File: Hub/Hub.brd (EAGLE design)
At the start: 85.9 x 24.9 mm, 9 parts

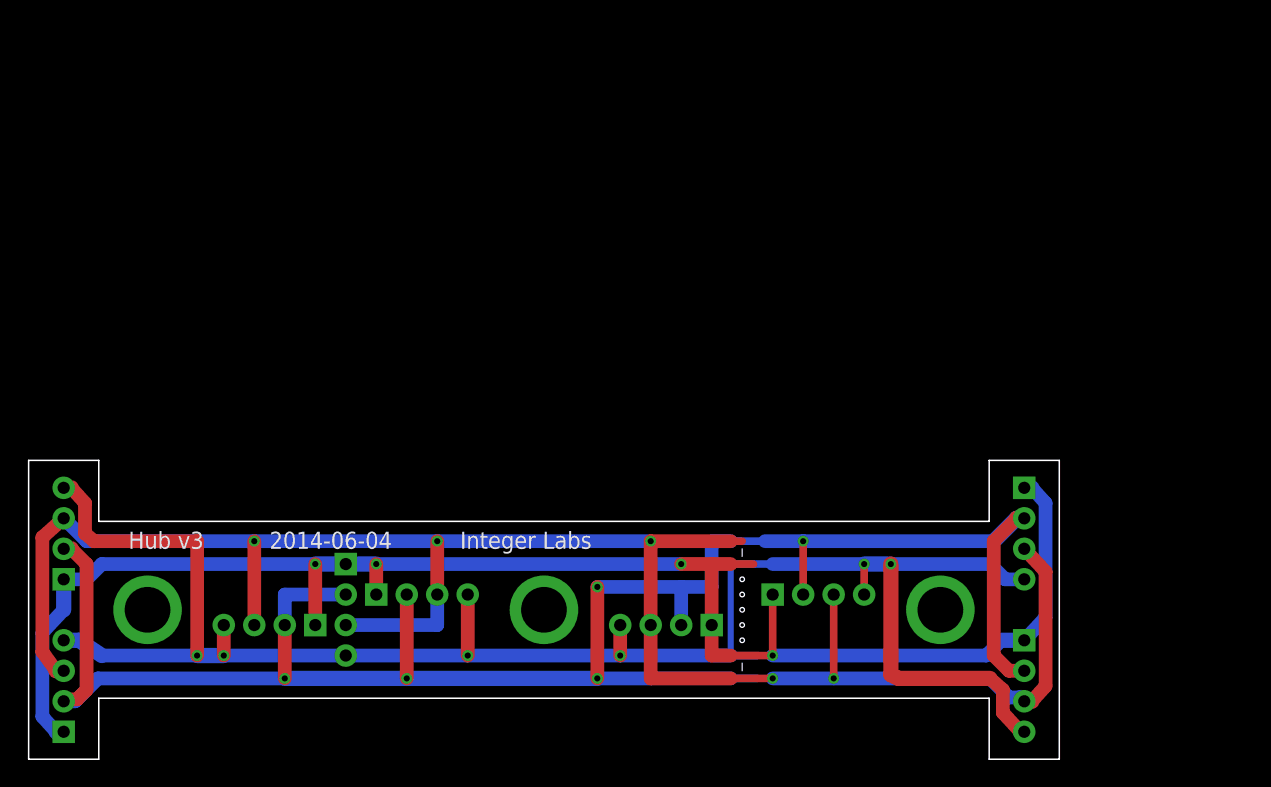
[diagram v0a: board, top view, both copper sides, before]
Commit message: Cleaned up pcb repository file structure.
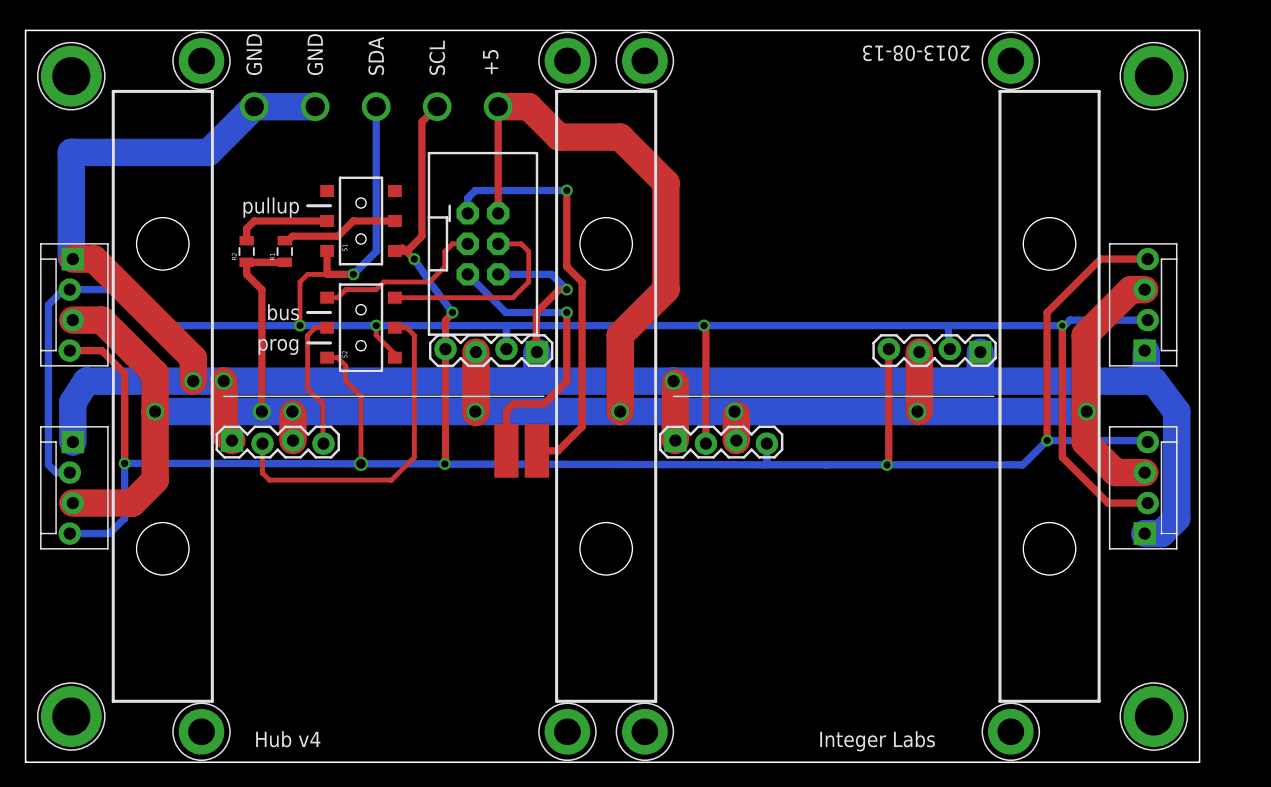
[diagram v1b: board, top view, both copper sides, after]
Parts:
- removed JP5, JP7, JP8: (no value), SparkFun-Connectors:1X04_NO_SILK
- added JP11, JP14: (no value), SparkFun-Connectors:1X04_LOCK
- added JP13: (no value), SparkFun-Connectors:2X3-SHROUDED
- added R1, R2: (no value), SparkFun-Resistors:0805
- added S1, S2: DPDT, SparkFun-Electromechanical:AYZ0202
- added U$1, U$2: SPRING-CONNECTOR, IntegerLabs:SPRING-CONNECTOR
- added U$10, U$11, U$12, U$13, U$14, U$7, U$8, U$9: HOLE#2, IntegerLabs:HOLE-#2
- added U$15, U$16, U$17, U$18, U$19: HOLETEST, IntegerLabs:HOLE-TEST
- added U$3, U$4, U$5, U$6: HOLE#4, IntegerLabs:HOLE-#4
- JP1, JP4: device SparkFun-Connectors:1X04_NO_SILK -> SparkFun-Connectors:1X04_LOCK
- JP2, JP3, JP6, JP9: device SparkFun-Connectors:1X04_NO_SILK -> SparkFun-Connectors:MOLEX-1X4_LOCK
- moved JP2 67.3 mm to (93.3, 34.3), turned to 90 degrees
- moved JP3 37.0 mm to (93.3, 19.1), turned to 90 degrees
- moved JP4 28.3 mm to (42.6, 34.3), turned to 180 degrees
- moved JP6 26.7 mm to (3.81, 41.9), turned to 270 degrees
- moved JP9 25.0 mm to (3.81, 26.7)
- moved JP1 16.7 mm to (17.2, 26.7), turned to 0 degrees
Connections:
- removed net N$1: JP1.4, JP2.4, JP3.4, JP4.4, JP5.4, JP6.4, JP7.4, JP8.4, JP9.4
- removed net N$2: JP1.3, JP2.3, JP3.3, JP4.3, JP5.3, JP6.3, JP7.3, JP8.3, JP9.3
- new net GND: JP1.1, JP11.1, JP13.6, JP14.1, JP2.1, JP3.1, JP4.1, JP6.1, JP9.1, U$15.P$1, U$16.P$1
- new net MISO: JP13.1, U$1.P$1
- new net MOSI: JP13.4, S2.6
- new net MOSI/SDA: JP1.2, S2.5
- new net RESET: JP13.5, U$2.P$1
- new net SCK: JP13.3, S2.3
- new net SCK/SCL: JP1.4, S2.2
- new net SCL: JP11.4, JP14.4, JP2.4, JP3.4, JP4.4, JP6.4, JP9.4, S1.4, S2.1, U$18.P$1
- new net SDA: JP11.2, JP14.2, JP2.2, JP3.2, JP4.2, JP6.2, JP9.2, S1.1, S2.4, U$17.P$1
- new net VCC: JP1.3, JP11.3, JP13.2, JP14.3, JP2.3, JP3.3, JP4.3, JP6.3, JP9.3, R1.1, R2.1, U$19.P$1
- net N$3: now also R1.2, S1.5; no longer JP1.2, JP2.2, JP3.2, JP4.2, JP5.2, JP6.2, JP7.2, JP8.2, JP9.2
- net N$4: now also R2.2, S1.2; no longer JP1.1, JP2.1, JP3.1, JP4.1, JP5.1, JP6.1, JP7.1, JP8.1, JP9.1
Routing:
- net VCC: track 0.00 -> 201.7 mm, vias 0 -> 8
- net GND: track 0.00 -> 187.3 mm, vias 0 -> 4
- net SCL: track 0.00 -> 186.2 mm, vias 0 -> 7
- net SDA: track 0.00 -> 173.4 mm, vias 0 -> 5
- net N$2: track 158.2 -> 0.00 mm, vias 5 -> 0
- net N$3: track 164.2 -> 9.85 mm, vias 5 -> 0
- net N$1: track 150.8 -> 0.00 mm, vias 6 -> 0
- net N$4: track 133.8 -> 7.97 mm, vias 4 -> 0
- net MISO: track 0.00 -> 34.6 mm, vias 0 -> 1
- net MOSI/SDA: track 0.00 -> 28.3 mm
- net RESET: track 0.00 -> 24.7 mm, vias 0 -> 1
- net MOSI: track 0.00 -> 17.0 mm
- net SCK: track 0.00 -> 14.3 mm
- net SCK/SCL: track 0.00 -> 11.9 mm
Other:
- board size 85.9 x 24.9 mm -> 97.8 x 61 mm
- board text added: "+5"
- board text added: "2013-08-13"
- board text added: "GND"
- board text added: "Hub v4"
- board text added: "SCL"
- board text added: "SDA"
- board text added: "bus"
- board text added: "prog"
- board text added: "pullup"
- board text removed: "2014-06-04"
- board text removed: "Hub v3"

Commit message: Latest version of schematics and boards
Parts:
- removed JP13: (no value), SparkFun-Connectors:2X3-SHROUDED
- removed JP9: (no value), SparkFun-Connectors:MOLEX-1X4_LOCK
- removed S1, S2: DPDT, SparkFun-Electromechanical:AYZ0202
- added C6: 10uF, SparkFun-Capacitors:EIA3528
- added F1: PTCSMD, SparkFun-PowerIC:PTC-1206
- added ICSP: (no value), SparkFun-Connectors:2X3
- added JP5: M023.5MM_LOCK, SparkFun-Connectors:SCREWTERMINAL-3.5MM-2_LOCK
- added LED1: (no value), led:CHIPLED_0805
- added Q1, Q2, Q5: BSS138, SparkFun-DiscreteSemi:SOT23
- added Q3, Q4: IRLML5203, transistor-power:MICRO3
- added Q6: TRANSISTOR-DUAL-PNP, IntegerLabs:SOT-26
- added Q7: SI2333DDS-T1-GE3, SparkFun-DiscreteSemi:SOT23-3
- added R3, R4: 2k, SparkFun-Passives:0805
- added R5, R6: (no value), SparkFun-Resistors:0805
- added R7, R8, R9: 2k, SparkFun-Resistors:0805
- added SJ1: SOLDERJUMPERNO, SparkFun-Passives:SJ_2S-NO
- added U$21: DC-JACK, IntegerLabs:DC-POWER-JACK
- added U$22, U$23, U$24: SPRING-CONNECTOR, IntegerLabs:SPRING-CONNECTOR
- added U$25, U$26, U$27: HOLE#2, IntegerLabs:HOLE-#2
- added U$28: HEADER-1X6MOLEX-KK254, IntegerLabs:HEADER-6POS-MOLEX-KK254
- JP2, JP3, JP6: value (none) -> HEADER-1X4MOLEX-SL; device SparkFun-Connectors:MOLEX-1X4_LOCK -> IntegerLabs:HEADER-1X4-MOLEX-SL
- R1: value (none) -> 2k
- R2: value (none) -> 390; device SparkFun-Resistors:0805 -> SparkFun-Passives:0805
- U$15: value HOLETEST -> HOLE#2; device IntegerLabs:HOLE-TEST -> IntegerLabs:HOLE-#2
- moved JP6 91.3 mm to (94.6, 32.4), turned to 90 degrees
- moved JP2 89.2 mm to (6.35, 14.6), turned to 270 degrees
- moved U$19 73.3 mm to (90.2, 1.78)
- moved U$16 66.2 mm to (90.2, 59.2)
- moved U$17 56.2 mm to (10.2, 1.78)
- moved R1 41.0 mm to (62.2, 47.6), flipped to the bottom
- moved U$15 36.4 mm to (43.2, 27.3)
- moved U$1 31.2 mm to (73.8, 27.9)
- moved U$2 28.7 mm to (68.7, 27.9)
- moved U$18 24.6 mm to (10.2, 59.2)
- moved U$5 3.81 mm to (97.8, 3.81)
- moved U$6 3.81 mm to (97.8, 57.1)
- moved R2 2.29 mm to (19.7, 40.6), flipped to the bottom
- moved JP1 1.91 mm to (19.1, 26.7)
- moved JP11 1.91 mm to (56.0, 26.7)
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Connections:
- removed net MOSI/SDA: JP1.2, S2.5
- removed net SCK/SCL: JP1.4, S2.2
- new net +3.3V: Q1.1, Q2.1, R3.2, R4.2, U$28.P$3
- new net N$1: Q3.1, Q4.1, Q5.3, R9.1, SJ1.2
- new net N$2: F1.1, JP5.2, U$21.P1
- new net N$5: F1.2, Q6.6, Q7.3
- new net N$6: Q3.3, R7.1
- new net N$7: Q4.3, R8.1
- new net N$8: LED1.A, R2.1
- new net PU_EN: Q5.1, R1.2, U$28.P$6
- new net SCL3.3: Q1.2, R3.1, U$28.P$4
- new net SDA3.3: Q2.2, R4.1, U$28.P$2
- new net VPROG: ICSP.2, U$24.P$1
- net GND: now also C6.C, ICSP.6, JP2.P$1, JP3.P$1, JP5.1, JP6.P$1, LED1.C, Q5.2, R1.1, R5.2, R6.1, SJ1.1, U$21.P2, U$28.P$1; no longer JP13.6, JP2.1, JP3.1, JP6.1, JP9.1, U$15.P$1
- net MISO: now also ICSP.1; no longer JP13.1
- net MOSI: now also ICSP.4, U$23.P$1; no longer JP13.4, S2.6
- net N$3: now also Q6.1, Q6.2, Q6.3, Q7.1, R5.1; no longer R1.2, S1.5
- net N$4: now also Q6.4, R6.2; no longer R2.2, S1.2
- net RESET: now also ICSP.5; no longer JP13.5
- net SCK: now also ICSP.3, U$22.P$1; no longer JP13.3, S2.3
- net SCL: now also JP1.4, JP2.P$4, JP3.P$4, JP6.P$4, Q1.3, R8.2; no longer JP2.4, JP3.4, JP6.4, JP9.4, S1.4, S2.1
- net SDA: now also JP1.2, JP2.P$2, JP3.P$2, JP6.P$2, Q2.3, R7.2; no longer JP2.2, JP3.2, JP6.2, JP9.2, S1.1, S2.4
- net VCC: now also C6.A, JP2.P$3, JP3.P$3, JP6.P$3, Q3.2, Q4.2, Q6.5, Q7.2, R2.2, R9.2, U$28.P$5; no longer JP13.2, JP2.3, JP3.3, JP6.3, JP9.3, R1.1, R2.1
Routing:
- net VCC: track 201.7 -> 286.8 mm, vias 8 -> 9
- net N$2: track 0.00 -> 44.6 mm
- net SCL3.3: track 0.00 -> 44.1 mm, vias 0 -> 1
- net VPROG: track 0.00 -> 43.9 mm, vias 0 -> 1
- net GND: track 187.3 -> 146.6 mm, vias 4 -> 15
- net +3.3V: track 0.00 -> 39.3 mm, vias 0 -> 2
- net PU_EN: track 0.00 -> 37.5 mm, vias 0 -> 1
- net SDA3.3: track 0.00 -> 29.8 mm
- net N$1: track 0.00 -> 29.4 mm
- net SCK: track 14.3 -> 43.7 mm, vias 0 -> 1
- net MOSI/SDA: track 28.3 -> 0.00 mm
- net RESET: track 24.7 -> 50.6 mm
- net SDA: track 173.4 -> 196.3 mm, vias 5 -> 7
- net SCL: track 186.2 -> 207.2 mm, vias 7 -> 3
- net MOSI: track 17.0 -> 36.1 mm, vias 0 -> 1
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- added copper zone on layer 16, net GND
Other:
- board size 97.8 x 61 mm -> 101.6 x 61 mm
- board text added: "+"
- board text added: "+3.3"
- board text added: "+5V"
- board text added: "-"
- board text added: "Modulo"
- board text added: "PWR"
- board text added: "icsp"
- board text added: "pu"
- board text added: "scl"
- board text added: "sda"
- board text added: "v6 2013-10-09"
- board text removed: "2013-08-13"
- board text removed: "GND"
- board text removed: "Hub v4"
- board text removed: "SCL"
- board text removed: "SDA"
- board text removed: "bus"
- board text removed: "prog"
- board text removed: "pullup"

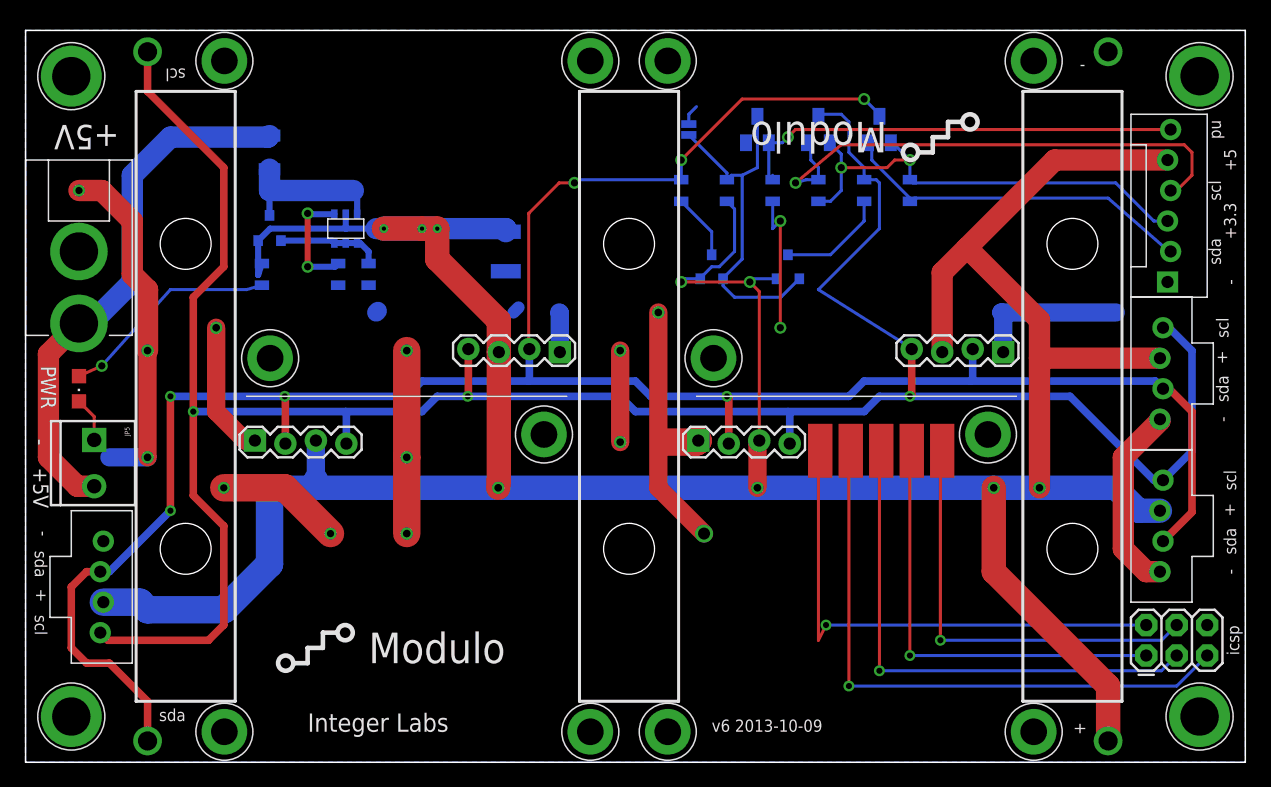
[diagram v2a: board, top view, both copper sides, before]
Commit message: New Hub with smaller form factor and bus connectors on bottom.
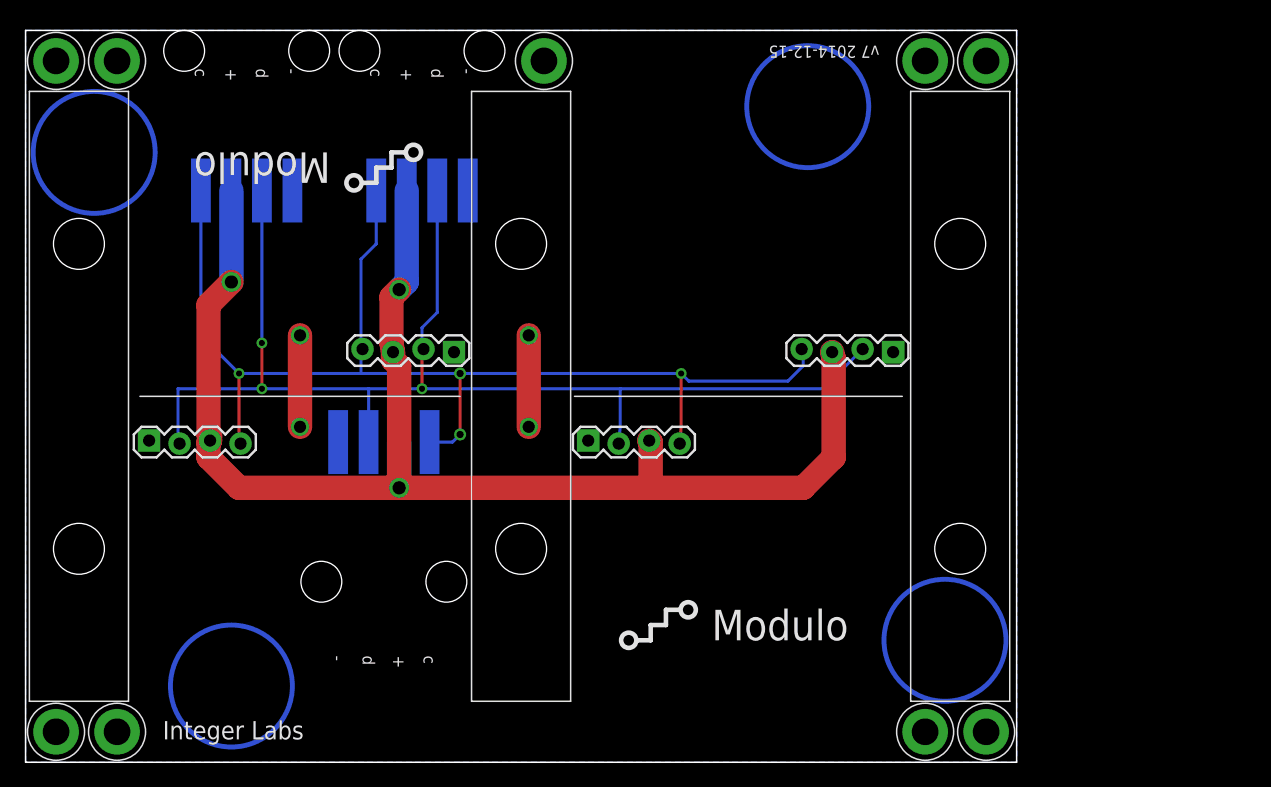
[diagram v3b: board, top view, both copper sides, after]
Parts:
- removed C6: 10uF, SparkFun-Capacitors:EIA3528
- removed F1: PTCSMD, SparkFun-PowerIC:PTC-1206
- removed ICSP: (no value), SparkFun-Connectors:2X3
- removed JP2, JP3, JP6: HEADER-1X4MOLEX-SL, IntegerLabs:HEADER-1X4-MOLEX-SL
- removed JP5: M023.5MM_LOCK, SparkFun-Connectors:SCREWTERMINAL-3.5MM-2_LOCK
- removed LED1: (no value), led:CHIPLED_0805
- removed Q1, Q2, Q5: BSS138, SparkFun-DiscreteSemi:SOT23
- removed Q3, Q4: IRLML5203, transistor-power:MICRO3
- removed Q6: TRANSISTOR-DUAL-PNP, IntegerLabs:SOT-26
- removed Q7: SI2333DDS-T1-GE3, SparkFun-DiscreteSemi:SOT23-3
- removed R1, R7, R8, R9: 2k, SparkFun-Resistors:0805
- removed R2: 390, SparkFun-Passives:0805
- removed R3, R4: 2k, SparkFun-Passives:0805
- removed R5, R6: (no value), SparkFun-Resistors:0805
- removed SJ1: SOLDERJUMPERNO, SparkFun-Passives:SJ_2S-NO
- removed U$1, U$2, U$22, U$23, U$24: SPRING-CONNECTOR, IntegerLabs:SPRING-CONNECTOR
- removed U$15, U$25, U$26, U$27: HOLE#2, IntegerLabs:HOLE-#2
- removed U$16, U$17, U$18, U$19: HOLETEST, IntegerLabs:HOLE-TEST
- removed U$21: DC-JACK, IntegerLabs:DC-POWER-JACK
- removed U$28: HEADER-1X6MOLEX-KK254, IntegerLabs:HEADER-6POS-MOLEX-KK254
- added X1, X2, X3: C-GRID-04-15-91, con-molex:15-91-04
- U$3, U$4, U$5: value HOLE#4 -> (none); device IntegerLabs:HOLE-#4 -> IntegerLabs:CARD-GUIDE-2"
- U$6: value HOLE#4 -> HOLE#2; device IntegerLabs:HOLE-#4 -> IntegerLabs:HOLE-#2
- moved U$10 76.4 mm to (7.62, 2.54)
- moved U$8 62.5 mm to (74.9, 58.4)
- moved U$14 56.0 mm to (80.0, 2.54)
- moved U$6 54.6 mm to (43.2, 58.4)
- moved U$4 46.0 mm to (41.3, 30.5)
- moved U$13 45.9 mm to (7.62, 58.4)
- moved U$5 33.3 mm to (77.9, 30.5)
- moved U$12 33.0 mm to (80.0, 58.4)
- moved U$3 26.7 mm to (4.45, 30.5)
- moved U$9 21.4 mm to (74.9, 2.54)
- moved U$11 14.0 mm to (2.54, 58.4)
- moved U$7 14.0 mm to (2.54, 2.54)
- moved JP11 9.17 mm to (46.9, 26.7)
- moved JP14 9.17 mm to (72.3, 34.3)
- moved JP4 8.81 mm to (35.7, 34.3)
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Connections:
- removed net +3.3V: Q1.1, Q2.1, R3.2, R4.2, U$28.P$3
- removed net MISO: ICSP.1, U$1.P$1
- removed net MOSI: ICSP.4, U$23.P$1
- removed net N$1: Q3.1, Q4.1, Q5.3, R9.1, SJ1.2
- removed net N$2: F1.1, JP5.2, U$21.P1
- removed net N$3: Q6.1, Q6.2, Q6.3, Q7.1, R5.1
- removed net N$4: Q6.4, R6.2
- removed net N$5: F1.2, Q6.6, Q7.3
- removed net N$6: Q3.3, R7.1
- removed net N$7: Q4.3, R8.1
- removed net N$8: LED1.A, R2.1
- removed net PU_EN: Q5.1, R1.2, U$28.P$6
- removed net RESET: ICSP.5, U$2.P$1
- removed net SCK: ICSP.3, U$22.P$1
- removed net SCL3.3: Q1.2, R3.1, U$28.P$4
- removed net SDA3.3: Q2.2, R4.1, U$28.P$2
- removed net VPROG: ICSP.2, U$24.P$1
- net GND: now also X1.1, X2.1, X3.1; no longer C6.C, ICSP.6, JP2.P$1, JP3.P$1, JP5.1, JP6.P$1, LED1.C, Q5.2, R1.1, R5.2, R6.1, SJ1.1, U$16.P$1, U$21.P2, U$28.P$1
- net SCL: now also X1.4, X2.4, X3.4; no longer JP2.P$4, JP3.P$4, JP6.P$4, Q1.3, R8.2, U$18.P$1
- net SDA: now also X1.2, X2.2, X3.2; no longer JP2.P$2, JP3.P$2, JP6.P$2, Q2.3, R7.2, U$17.P$1
- net VCC: now also X1.3, X2.3, X3.3; no longer C6.A, JP2.P$3, JP3.P$3, JP6.P$3, Q3.2, Q4.2, Q6.5, Q7.2, R2.2, R9.2, U$19.P$1, U$28.P$5
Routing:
- net VCC: track 286.8 -> 119.6 mm, vias 9 -> 3
- net GND: track 146.6 -> 15.2 mm, vias 15 -> 4
- net SCL: track 207.2 -> 101.3 mm, vias 3 -> 4
- net SDA: track 196.3 -> 105.9 mm, vias 7 -> 3
- net RESET: track 50.6 -> 0.00 mm, vias 1 -> 0
- net N$2: track 44.6 -> 0.00 mm
- net SCL3.3: track 44.1 -> 0.00 mm, vias 1 -> 0
- net VPROG: track 43.9 -> 0.00 mm, vias 1 -> 0
- net SCK: track 43.7 -> 0.00 mm, vias 1 -> 0
- net +3.3V: track 39.3 -> 0.00 mm, vias 2 -> 0
- net PU_EN: track 37.5 -> 0.00 mm, vias 1 -> 0
- net MISO: track 36.8 -> 0.00 mm, vias 1 -> 0
- net MOSI: track 36.1 -> 0.00 mm, vias 1 -> 0
- net SDA3.3: track 29.8 -> 0.00 mm
- net N$1: track 29.4 -> 0.00 mm
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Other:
- board size 101.6 x 61 mm -> 82.5 x 61 mm
- board text added: "c"
- board text added: "d"
- board text added: "v7 2014-12-15"
- board text removed: "+3.3"
- board text removed: "+5"
- board text removed: "+5V"
- board text removed: "PWR"
- board text removed: "icsp"
- board text removed: "pu"
- board text removed: "scl"
- board text removed: "sda"
- board text removed: "v6 2013-10-09"

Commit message: various minor changes
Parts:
- added JP2, JP3, JP5, JP6, JP7, JP8: (no value), SparkFun-Connectors:1X04_LOCK
- moved X2 16.1 mm to (16.9, 58.4)
- moved X1 12.7 mm to (31.1, 58.4)
- moved X3 7.85 mm to (22.2, 17.8), turned to 90 degrees
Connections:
- net GND: now also JP2.1, JP3.1, JP5.1, JP6.1, JP7.1, JP8.1
- net SCL: now also JP2.4, JP3.4, JP5.4, JP6.4, JP7.4, JP8.4
- net SDA: now also JP2.2, JP3.2, JP5.2, JP6.2, JP7.2, JP8.2
- net VCC: now also JP2.3, JP3.3, JP5.3, JP6.3, JP7.3, JP8.3
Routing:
- net SDA: track 105.9 -> 153.3 mm, vias 3 -> 2
- net GND: track 15.2 -> 60.7 mm, vias 4 -> 2
- net SCL: track 101.3 -> 143.9 mm, vias 4 -> 0
- net VCC: track 119.6 -> 157.2 mm, vias 3 -> 0
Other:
- board text added: "v7"
- board text removed: "+"
- board text removed: "-"
- board text removed: "c"
- board text removed: "d"
- board text removed: "v7 2014-12-15"

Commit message: Checkpointing PCB designs
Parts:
- added C1, C2, C3, C4: 68uF, SparkFun-Capacitors:1210
- added F1: (no value), SparkFun-Passives:0805
- added LED1: (no value), adafruit:CHIP-LED0805
- added Q2: DMMT5401, IntegerLabs:SOT-26
- added Q3: DMG2305UX, transistor-power:MICRO3
- added R2: 680, SparkFun-Passives:0805
- added R5: 10k 1%, SparkFun-Passives:0805
- added R9: 47k 1%, SparkFun-Passives:0805
- added U$1: DC-JACKLOWPRO, IntegerLabs:DC-POWER-JACK-LOWPRO
- moved X1 2.13 mm to (33.0, 57.5)
- moved X2 1.35 mm to (17.8, 57.5)
- moved U$3 0.25 mm to (4.70, 30.5)
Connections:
- new net N$1: F1.2, U$1.1
- new net N$14: Q2.1, Q2.2, Q2.3, R5.2
- new net N$16: Q2.4, Q3.1, R9.2
- new net N$8: LED1.A, R2.1
- new net VREG: F1.1, Q2.6, Q3.3
- net GND: now also C1.2, C2.2, C3.2, C4.2, LED1.C, R5.1, R9.1, U$1.2
- net VCC: now also C1.1, C2.1, C3.1, C4.1, Q2.5, Q3.2, R2.2
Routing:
- net VCC: track 157.2 -> 186.1 mm
- net N$8: track 0.00 -> 11.8 mm
- net VREG: track 0.00 -> 4.98 mm
- net N$1: track 0.00 -> 3.95 mm
- net N$14: track 0.00 -> 3.89 mm
- net N$16: track 0.00 -> 3.74 mm
- net GND: track 60.7 -> 63.5 mm
- net SDA: track 153.3 -> 151.6 mm
- net SCL: track 143.9 -> 142.5 mm
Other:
- board text added: "5V"
- board text added: "power"
- board text added: "v8"
- board text removed: "v7"
